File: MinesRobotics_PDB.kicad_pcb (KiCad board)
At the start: 2 copper layers, 101.1 x 75.9 mm, 57 parts, among them J1 Conn_01x02_Female, J2 Conn_01x02_Female, J3 Conn_01x02_Female, J4 Conn_01x02_Female, J5 Conn_01x02_Female, J6 Conn_01x02_Female, J7 Conn_01x02_Female, J8 Conn_01x02_Female, J9 Conn_01x02_Female, U1 I6A4W020A033V-003-R

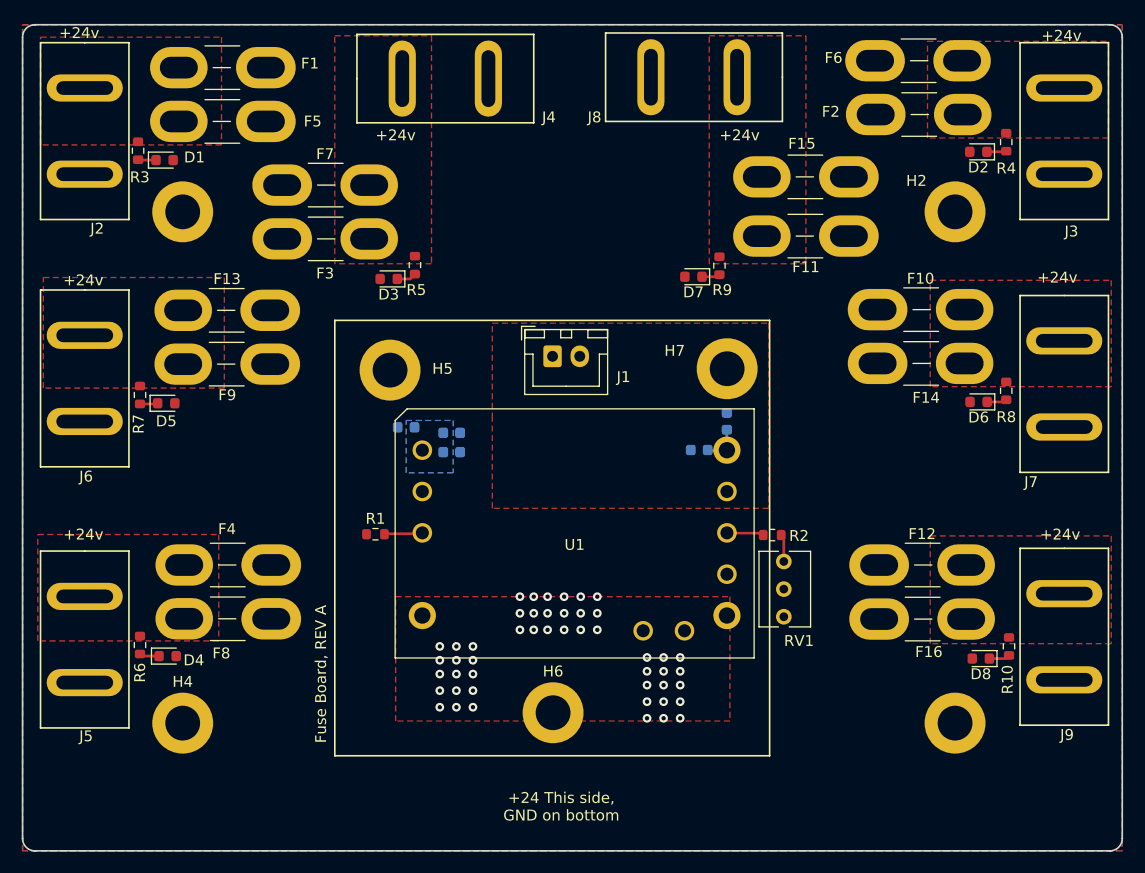
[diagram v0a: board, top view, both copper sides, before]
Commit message: No point using Fuses w/o fuse holders, Also added 3D models
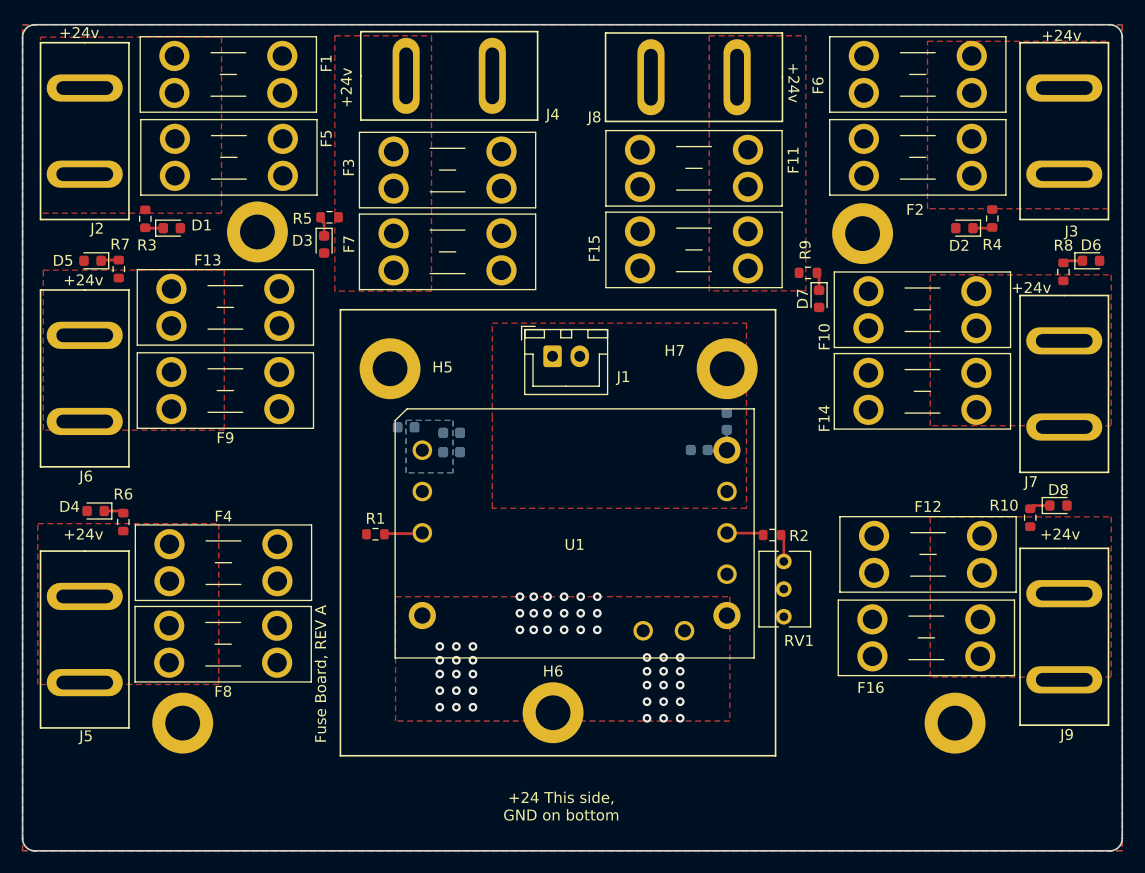
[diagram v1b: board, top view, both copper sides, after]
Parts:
- F1, F10, F11, F12, F13, F14, F15, F16, F2, F3, F4, F5, F6, F7, F8, F9: footprint Fuse:Fuse_Blade_Mini_directSolder -> Fuse:Fuseholder_Blade_Mini_Keystone_3568
- J3, J4, J5, J6, J8: value Conn_01x02_Female -> AndersonPowerPole
- moved F7 21.6 mm to (125.3, 73.4), turned to 180 degrees
- moved F11 20.8 mm to (138.0, 62.3), turned to 0 degrees
- moved F3 20.7 mm to (125.3, 65.9), turned to 180 degrees
- moved F15 19.8 mm to (138.0, 69.8), turned to 0 degrees
- moved D6 16.6 mm to (179.5, 72.5), turned to 0 degrees
- moved D8 15.8 mm to (176.5, 95.0), turned to 0 degrees
- moved D4 14.9 mm to (88.0, 95.5), turned to 180 degrees
- moved D5 14.7 mm to (87.7, 72.5), turned to 180 degrees
- moved R8 12.1 mm to (177.0, 73.5), turned to -90 degrees
- moved R10 12.0 mm to (173.9, 96.1), turned to -90 degrees
- moved R7 11.7 mm to (90.1, 73.3), turned to -90 degrees
- moved D7 11.7 mm to (154.5, 76.0), turned to -90 degrees
- moved R6 11.4 mm to (90.5, 96.5), turned to -90 degrees
- moved R5 9.00 mm to (109.5, 68.5), turned to 0 degrees
- moved H2 8.73 mm to (158.5, 70.0)
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
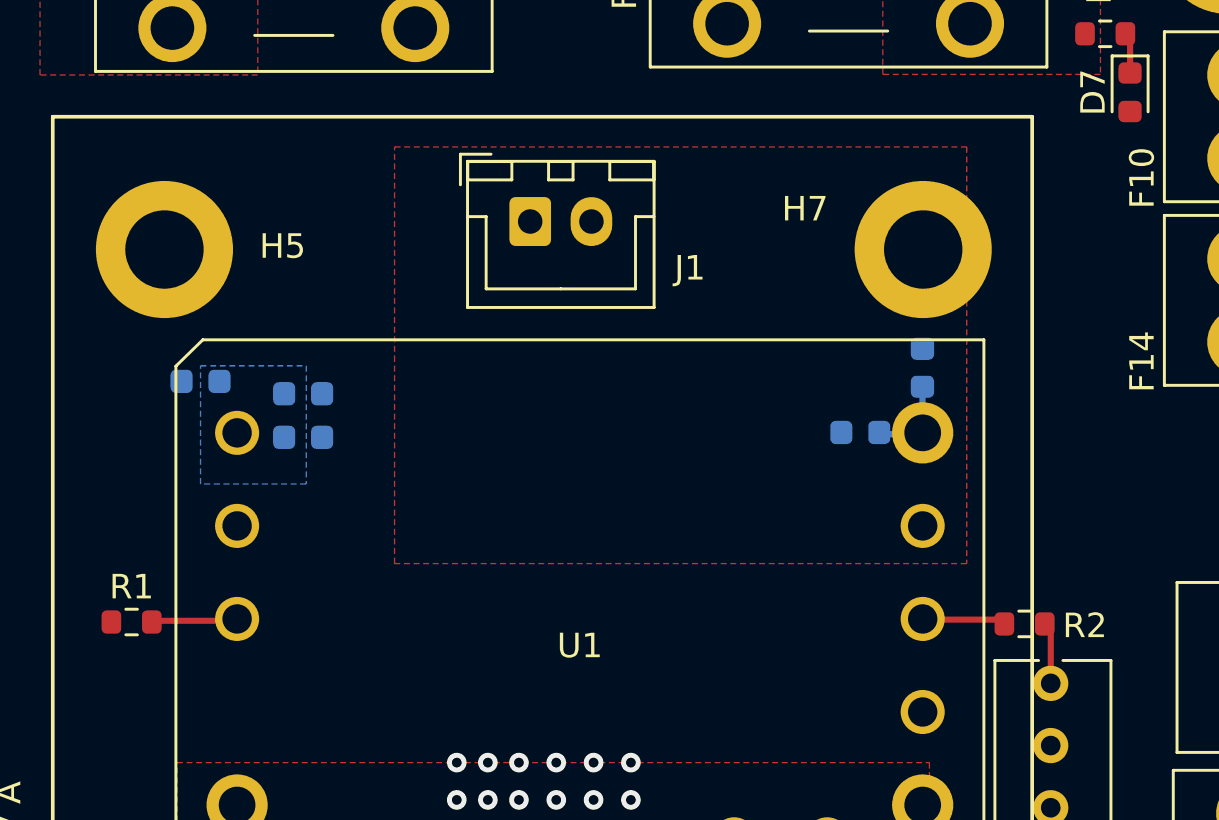
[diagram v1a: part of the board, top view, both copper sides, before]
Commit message: Added BOM and updated Cap footprint according to availability
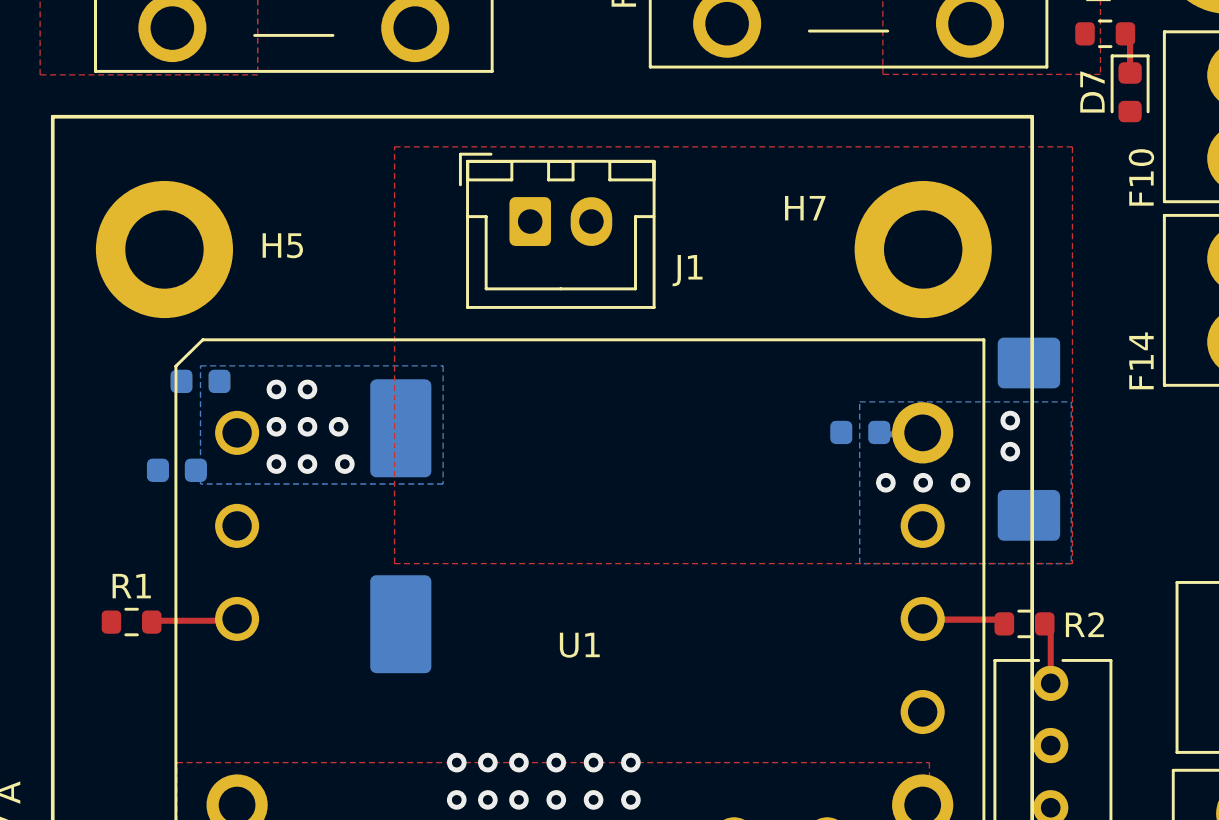
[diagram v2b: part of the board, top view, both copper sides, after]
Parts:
- C1: footprint Capacitor_SMD:C_0603_1608Metric -> Capacitor_SMD:CP_Elec_10x10
- C3: footprint Capacitor_SMD:C_0603_1608Metric -> Capacitor_Tantalum_SMD:CP_EIA-7343-15_Kemet-W
- J3, J4, J5, J6, J8: value AndersonPowerPole -> Conn_01x02_Female
- moved C8 6.03 mm to (115.6, 91.4), turned to 180 degrees
- moved C1 5.39 mm to (124.7, 93.7), turned to -90 degrees
- moved C3 5.24 mm to (150.4, 90.2)
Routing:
- net +9V: track 3.81 -> 1.89 mm, vias 0 -> 5
- net +24V: vias 0 -> 8
- added copper zone on B.Cu, net +9V

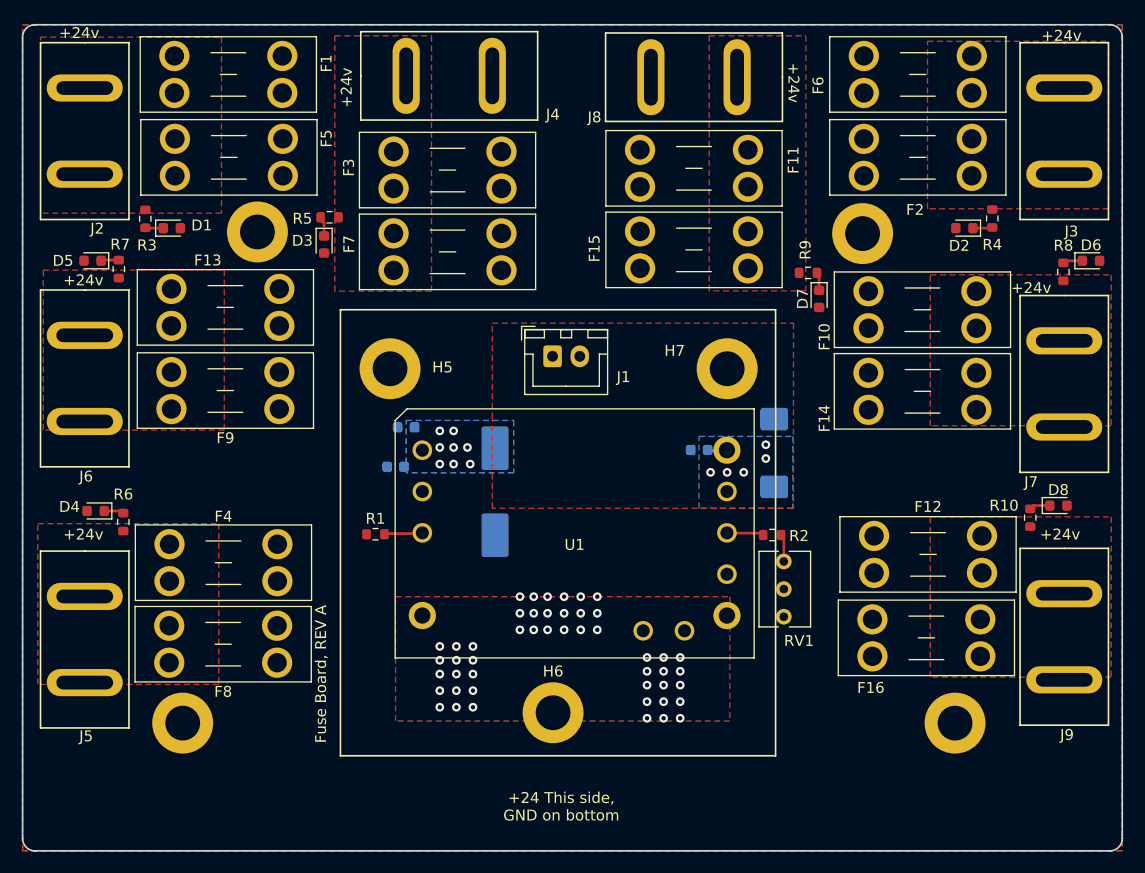
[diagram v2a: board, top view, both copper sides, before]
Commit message: Changed resistors and LEDs to 0805 and updated Production files
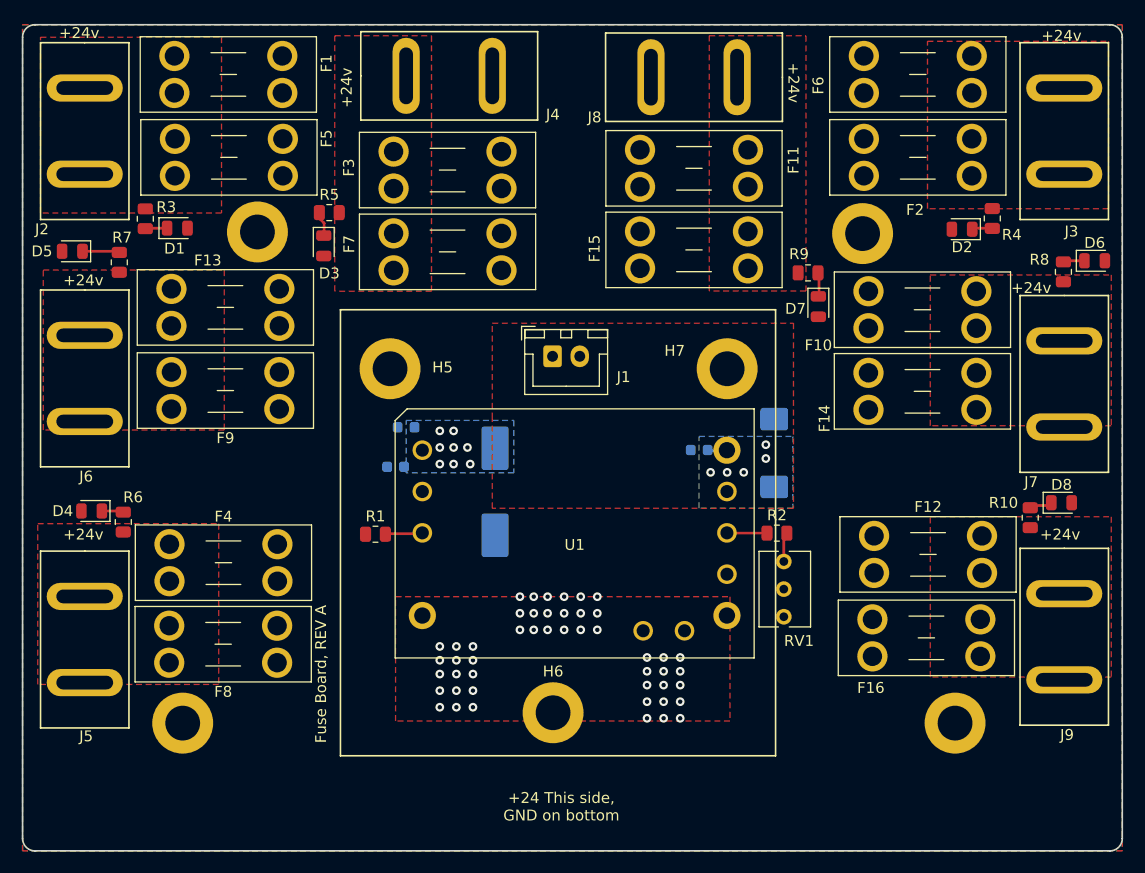
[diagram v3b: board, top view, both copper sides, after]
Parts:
- D1, D2, D3, D4, D5, D6, D7, D8: footprint LED_SMD:LED_0603_1608Metric -> LED_SMD:LED_0805_2012Metric
- R1, R10, R2, R3, R4, R5, R6, R7, R8, R9: footprint Resistor_SMD:R_0603_1608Metric -> Resistor_SMD:R_0805_2012Metric
- moved D5 2.05 mm to (85.9, 71.6)
- moved D7 0.71 mm to (154.4, 76.7)
- moved R7 0.62 mm to (90.2, 72.6)
- moved D1 0.50 mm to (95.5, 69.5)
- moved R2 0.47 mm to (150.6, 97.5)
- moved R5 0.43 mm to (109.5, 68.1)
- moved D8 0.38 mm to (176.8, 94.7)
- moved D4 0.37 mm to (87.6, 95.5)
- moved D6 0.33 mm to (179.8, 72.5)
- moved D2 0.24 mm to (167.6, 69.6)
- moved D3 0.12 mm to (109.0, 71.1)
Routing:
- net Net-(D5-Pad1): track 1.65 -> 3.42 mm
